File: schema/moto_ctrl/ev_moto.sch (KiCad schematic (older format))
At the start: 18 parts

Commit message: Added analog part of revolution motor control.
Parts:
- added C30, C33, C40: 100n, symbol C
- added C31, C38, C42, C43: 10u, symbol C
- added C36: C, symbol C
- added C37: 1u, symbol C
- added C39: 2.2n, symbol C
- added C41: 1m, symbol C
- added D4: AD8607, symbol AD8607
- added D5: 1N5819, symbol DIODESCH
- added D6, D7: LED, symbol LED
- added J3: DB9, symbol DB9
- added L2: INDUCTOR, symbol INDUCTOR
- added P6, P8: CONN_2, symbol CONN_2
- added P9: SWD-IAP, symbol CONN_5
- added Q1, Q2: bc847, symbol NPN
- added R66, R67, R68, R69, R70, R78, R84, R90: 10k, symbol R
- added R71, R73, R74, R86, R89, R91, R92: 50, symbol R
- added R76, R79: 100, symbol R
- added R77, R83: 1k, symbol R
- added R80, R81, R82: 1R5, symbol R
- added R85: 30k, symbol R
- added R87, R88: 500, symbol R
- added U3: NCP3063, symbol NCP3063
- added adc1: AD5300, symbol AD5300
- gave numbers to parts that had none: 18
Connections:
- net labels added: +5v, 5v-out, dac-din, dac-out, dac-sclk, dir+, dir-, dir-input, en+, en-, en-input, enc-clock, enc-data, out-buf, out-gain, ~dac-synch~
- net labels removed: i-1-1, i-1-2, i-2-1, i-2-2, i-3-1, i-3-2, i-4-1, i-4-2, io-1-1, io-1-2, io-2-1, io-2-2, io-3-1, io-3-2, io-4-1, io-4-2, scl, sda, sensor-1, sensor-2, sensor-3, sensor-4, synch, usb-d+, usb-d-
- wire segments 95 -> 242
- no-connect marks 7 -> 24
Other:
- note added: "Driver power socket (output)"
- note added: "Here it should be either \nupper or lower one depending \non which output is used."
- note added: "High power input"

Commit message: Added all possible ways of control of BMSD controller.
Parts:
- removed Q1, Q2: bc847, symbol NPN
- removed R67: 10k, symbol R
- added C33: 220n, symbol C
- added C39: 100n, symbol C
- added C40: 10u, symbol C
- added Q1, Q4: MOSFET_P, symbol MOSFET_P
- added Q2, Q6: MOSFET_N, symbol MOSFET_N
- added Q3, Q5: NPN, symbol NPN
- added R101, R104, R112, R85, R90, R95: 1k, symbol R
- added R105, R109, R83, R91, R92, R97: 100, symbol R
- added R110, R64, R65, R71, R73, R82, R94, R96: 10k, symbol R
- added rs3: STM3485EBDR, symbol STM3485EBDR
- C36: renamed from C37; value 1u -> 220n
- renumbered C36 to C30, C30 to C31, C31 to C32, C32 to C34, C33 to C35, C34 to C37, C35 to C38, C38 to C42, C39 to C43, C40 to C44, C41 to C45, C42 to C46, C43 to C47, D6 to D5, D7 to D6, D5 to D7, R90 to R100, R89 to R102, R79 to R103, R83 to R106, R91 to R107, R92 to R108, R84 to R111, R64 to R66, R66 to R67, R69 to R68, R70 to R69, R68 to R70, R65 to R72, R71 to R74, R72 to R75, R73 to R76, R74 to R77, R75 to R78, R87 to R80, R88 to R81, R76 to R84, R80 to R86, R81 to R87, R82 to R88, R77 to R89, R78 to R93, R85 to R98, R86 to R99
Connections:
- net labels added: bmsd-dir, bmsd-rx, bmsd-tx, rs-a, rs-b
- net labels removed: out-buf
- wire segments 242 -> 300
- no-connect marks 24 -> 21
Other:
- note added: "Absolute encoder RS-485 readout."
- note added: "BMSD control"
- note added: "First stage: w = 1/(10e4 * 220e-9) = 455 (1/s)\nf = 72Hz"
- note added: "H(s) = 1/(1 + s*R65*C33) * (3 + s*R*C36)/(2 + s*R*C36)"
- note added: "Second stage: 16*(9+w^2*R^2*C^2)=25*(4+w^2*R^2*C^2)\nw = 1005 (1/s)\nf = 160Hz"
- note added: "This is RS-485 BMSD control part."
- note added: "This part if \nnegative pads \nare grounded.\n\nRs on ends are just \nfor avoiding DRC errors."
- note added: "This part if \npositive pads \nare +5V powered.\n\nRs on ends are just \nfor avoiding DRC errors."
- note added: "Two stages amplifier.\nFirst is buffer with infinite input \nR because DAC can't give big \ncurrent. After that RC low pass.\nAnd last stage is x1.5 at 0Hz and \nx1 at (inf) Hz amplifier with cutoff \nat about 500Hz."
- note removed: "Here it should be either \nupper or lower one depending \non which output is used."
- moved on the sheet: C30, C36, D4, D5, D6, P8, P9, R102, R103, R106, R107, R108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

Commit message: Added analog outputs for escon 50/5 controls, rs-485 inputs for encoder signals recognition and DB-9 sockets for encoder inputs.
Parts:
- added C41, C48, C50, C51, C53, C54, C56, C57, C58, C60, C61, C62, C63, C72, C73: 100n, symbol C
- added C49, C52, C55, C59: 10u, symbol C
- added C64, C65, C66, C67, C68, C69, C70, C71: 220n, symbol C
- added D8, D9: AD8607, symbol AD8607
- added J4, J5, J6, J7: DB9, symbol DB9
- added R113, R114, R115, R124, R125, R126, R127, R128, R129, R130, R131, R132, R133, R134, R135, R136, R137, R138, R139, R140, R141, R142, R143, R144, R145, R146, R147, R148, R79: 10k, symbol R
- added R116, R117, R118, R119, R120, R121, R122, R123: 50, symbol R
- added adc2, adc3, adc4, adc5: AD5300, symbol AD5300
- added rs10, rs11, rs4, rs5, rs6, rs7, rs8, rs9: STM3485EBDR, symbol STM3485EBDR
- C30: value C -> 100n
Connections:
- net labels added: A1, A1+, A1-, A2, A2+, A2-, A3, A3+, A3-, A4, A4+, A4-, B1, B1+, B1-, B2, B2+, B2-, B3, B3+, B3-, B4, B4+, B4-, analog-out1, analog-out2, analog-out3, analog-out4, ~analog1-cs~, ~analog2-cs~, ~analog3-cs~, ~analog4-cs~
- wire segments 300 -> 602
- no-connect marks 21 -> 17
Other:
- note added: "For manipulator encoder inputs \nand outputs. The common sense of \nshorted neighbour pins is to wire \nencoder signals to controller board \nand to escon 50/5 controller simultaneously."
- note added: "Manipulator encoders readout."

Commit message: Only another DB-37 suits size. Also should think for a while about rebolving motor encoder's socket.
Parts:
- removed J4, J5, J6, J7: DB9, symbol DB9
- added J4: DB37, symbol DB37
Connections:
- no-connect marks 17 -> 18

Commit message: Schema edited. Have to leave just tow manipulator controls on one board. So it will be two boards for total control. Painted PCB edge with placment holes identical to previous valve_2 PCB.
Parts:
- removed C25: CP1, symbol CP1
- removed C53, C54, C57, C58, C62, C63, C72: 100n, symbol C
- removed C55, C59: 10u, symbol C
- removed C66, C67, C69, C71: 220n, symbol C
- removed D9: AD8607, symbol AD8607
- removed J3: DB9, symbol DB9
- removed P5, P6: CONN_2, symbol CONN_2
- removed R120, R121, R122, R123: 50, symbol R
- removed R124, R125, R127, R128, R131, R132, R135, R136, R139, R140, R142, R144, R146, R148: 10k, symbol R
- removed adc4, adc5: AD5300, symbol AD5300
- removed rs10, rs11, rs8, rs9: STM3485EBDR, symbol STM3485EBDR
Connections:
- net labels removed: A3, A3+, A3-, A4, A4+, A4-, B3, B3+, B3-, B4, B4+, B4-, analog-out3, analog-out4, ~analog3-cs~, ~analog4-cs~
- wire segments 602 -> 452
- no-connect marks 18 -> 22
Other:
- note added: "BMSD related \nabsolute encoder."
- note added: "Encoder connection socket.\nIt is duplicated on 37-pin socket.\nJust not sure I'll be able to find \nit anywhere."
- note removed: "Driver power socket (output)"
- note removed: "Encoder connection socket"
- note removed: "High power input"
- moved on the sheet: C60, C61, C64, C65, C68, C70, C73, D8, P7, R129, R130, R133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

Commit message: Started routing. At the moment don't know where I should put clemmas power. Probably replace D-SUB-9 with them.
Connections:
- net labels added: addr1, addr2, addr3
- wire segments 452 -> 455
- no-connect marks 22 -> 19

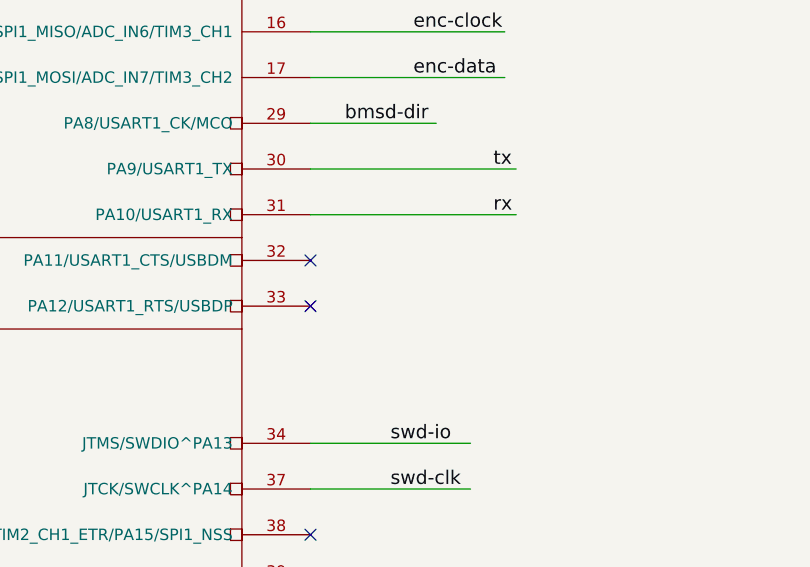
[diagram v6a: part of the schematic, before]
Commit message: Placing elements.
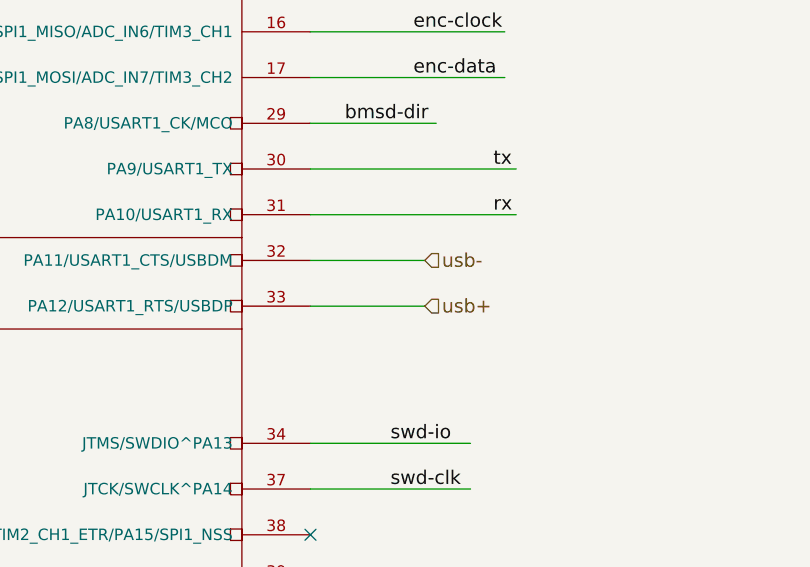
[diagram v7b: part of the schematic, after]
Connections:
- net labels added: usb+, usb-
- wire segments 455 -> 457
- no-connect marks 19 -> 17
